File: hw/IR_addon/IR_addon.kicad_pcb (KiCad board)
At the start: 2 copper layers, 89.6 x 55 mm, 90 parts, among them J1 CONN_02X08, J10 CONN_01X01, J11 CONN_01X01, J12 CONN_01X01, J13 CONN_01X01, J14 CONN_01X01, J15 CONN_01X01, J16 CONN_01X01, J17 CONN_01X01, J18 CONN_01X01, J19 CONN_01X01, J2 CONN_02X08, J20 CONN_01X01, J21 CONN_01X01, J22 CONN_01X01, J23 CONN_01X01, J24 CONN_01X01, J25 CONN_01X01, J26 CONN_01X01, J27 CONN_01X01, J28 CONN_01X01, J29 CONN_01X01, J3 CONN_01X02, J30 CONN_01X01, J31 CONN_01X01, J32 CONN_01X01, J33 CONN_01X01, J34 CONN_01X01, J35 CONN_01X01, J36 CONN_01X01, J37 CONN_01X01, J38 CONN_01X01, J39 CONN_01X01, J40 CONN_01X01, J41 CONN_02X03, J42 CONN_01X15, J43 CONN_01X15, J44 USB_B_Mini, J9 CONN_01X01, SW1 SwitchPush, U1 ATmega328P-AU, U2 FT230XQ, Y1 16MHz

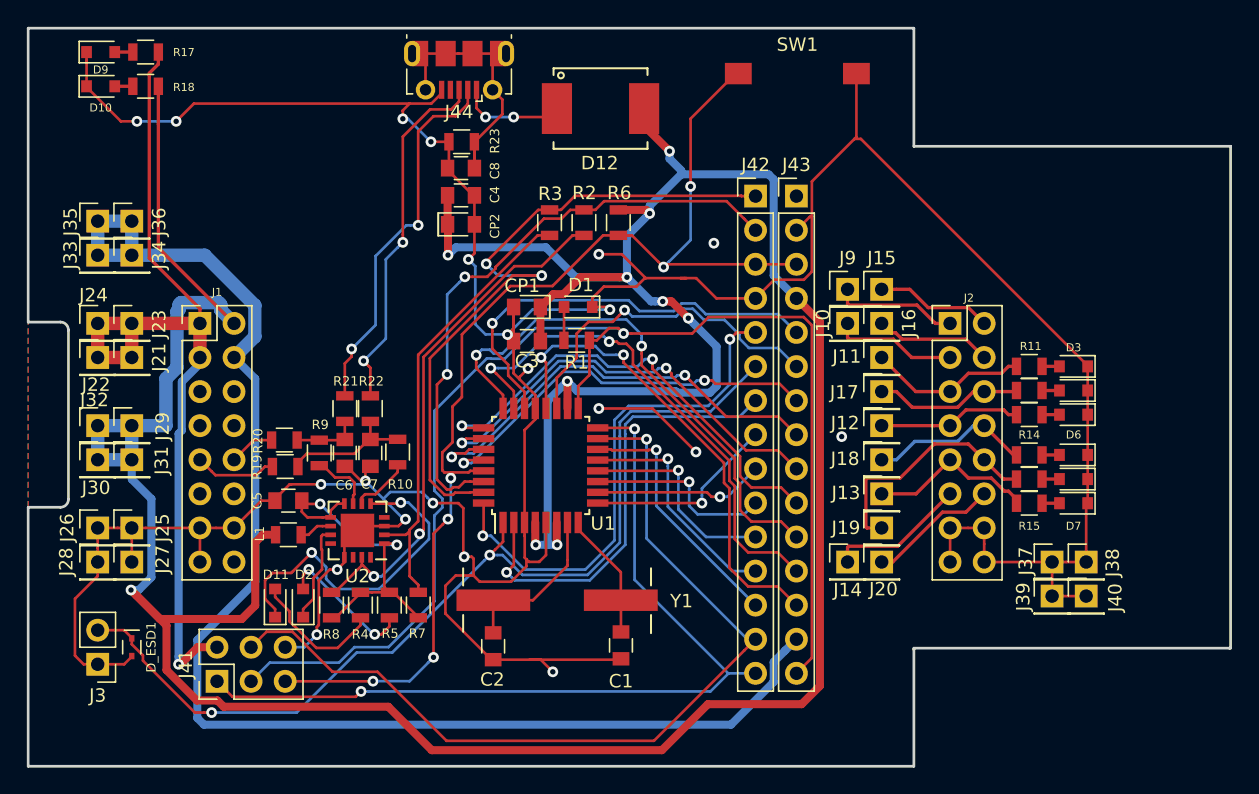
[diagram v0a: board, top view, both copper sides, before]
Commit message: Various fixes in schematics and PCB design
What has been done:

* Replace FT230XQ with FT232RQ
* Adapt schematics to new FTDI chip
* Rearrange texts on F.Mask layer
* Add smaller schottky diode next to usb
* Add load resistor for IR LED
* Move capacitors further from XTAL
* Rearrange overlapping texts on F.Silk layer

Doubts:

* Maybe we should remove uUSB from PCB, since all we are using
  are USB lines from MuxPi. As for now uUSB was never used.

Change-Id: Icd19173fda610c0574442d99b39109bb18bf1090
Signed-off-by: Katarzyna Gorska <k.gorska@samsung.com>
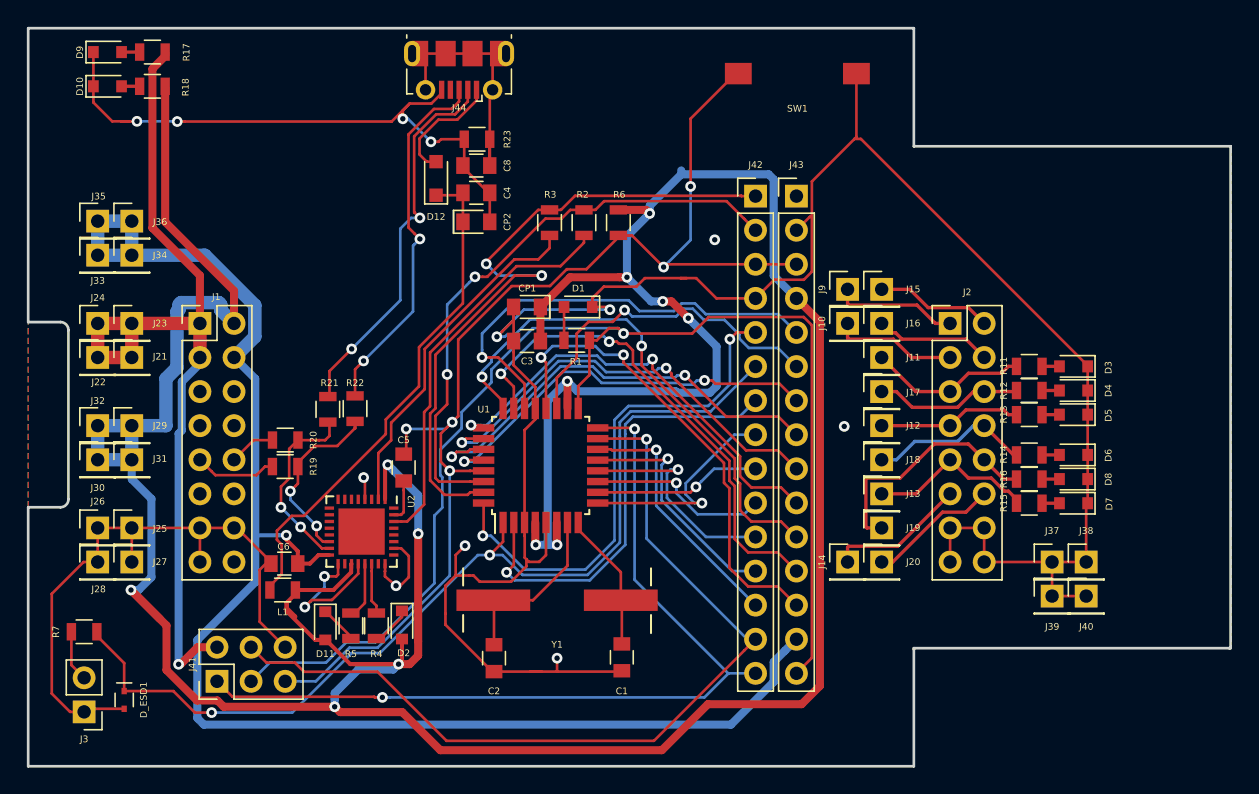
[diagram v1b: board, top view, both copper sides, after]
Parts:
- removed C7: 47pF/50V, Muxpi Addon:C_0805
- removed R10, R9: 27R, Muxpi Addon:R_0805
- removed R8: 10k, Muxpi Addon:R_0805
- C1, C2, C3, C4, C5, C8: footprint Muxpi Addon:C_0805 -> Muxpi_footprints:C_0805
- C6: value 47pF/50V -> 0.1uF; footprint Muxpi Addon:C_0805 -> Muxpi_footprints:C_0805
- CP1, CP2: footprint Muxpi Addon:C_T_0805 -> Muxpi_footprints:C_T_0805
- D1, D10, D11, D3, D4, D5, D6, D7, D8, D9: footprint Diodes_SMD:D_0805 -> Muxpi_footprints:D_0805
- D12: value MBRS410L -> BAT60B; footprint Muxpi Addon:403AC -> Muxpi_footprints:D_SOD-323_HandSoldering
- D2: value KPT-2012SGC -> KPT-2012EC; footprint Diodes_SMD:D_0805 -> Muxpi_footprints:D_0805
- D_ESD1: footprint Muxpi Addon:SOD-523 -> Muxpi_footprints:SOD-523
- J1, J2: footprint Pin_Headers:Pin_Header_Straight_2x08_Pitch2.54mm -> Muxpi_footprints:Pin_Header_Straight_2x08_Pitch2.54mm
- J10, J11, J12, J13, J14, J15, J16, J17, J18, J19, J20, J21, J22, J23, J24, J25, J26, J27, J28, J29, J30, J31, J32, J33, J34, J35, J36, J37, J38, J39, J40, J9: footprint Pin_Headers:Pin_Header_Straight_1x01_Pitch2.54mm -> Muxpi_footprints:Pin_Header_Straight_1x01_Pitch2.54mm
- J3: footprint Pin_Headers:Pin_Header_Straight_1x02_Pitch2.54mm -> Muxpi_footprints:Pin_Header_Straight_1x02_Pitch2.54mm
- J41: footprint Muxpi Addon:Pin_Header_Straight_2x03_Pitch2.54mm -> Muxpi_footprints:Pin_Header_Straight_2x03_Pitch2.54mm
- J42, J43: footprint Muxpi Addon:Pin_Header_Straight_1x15_Pitch2.54mm -> Muxpi_footprints:Pin_Header_Straight_1x15_Pitch2.54mm
- J44: footprint Muxpi Addon:USB_Micro-B_Molex-105017-0001 -> Muxpi_footprints:USB_Micro-B_Molex-105017-0001
- L1, R1, R19, R2, R20, R22, R23, R3, R6: footprint Muxpi Addon:R_0805 -> Muxpi_footprints:R_0805
- R11, R12, R13, R14, R15, R16, R17, R18: footprint Resistors_SMD:R_0805 -> Muxpi_footprints:R_0805
- R21: value 0 -> 330R; footprint Muxpi Addon:R_0805 -> Muxpi_footprints:R_0805
- R4, R5: value 560R -> 330R; footprint Muxpi Addon:R_0805 -> Muxpi_footprints:R_0805
- R7: value 10k -> R; footprint Muxpi Addon:R_0805 -> Muxpi_footprints:R_0805
- SW1: footprint Muxpi Addon:DTSM-3 -> Muxpi_footprints:DTSM-3
- U1: footprint Muxpi Addon:TQFP-32_7x7mm_Pitch0.8mm -> Muxpi_footprints:TQFP-32_7x7mm_Pitch0.8mm
- U2: value FT230XQ -> FT232RQ; footprint Muxpi Addon:QFN-16-1EP_4x4mm_Pitch0.65mm -> Muxpi_footprints:QFN-32-1EP_5x5mm_Pitch0.5mm
- Y1: footprint Muxpi Addon:HC49USM -> Muxpi_footprints:HC49USM
- moved R7 25.0 mm to (73.5, 179.6), turned to 180 degrees
- moved D12 13.3 mm to (99.7, 145.8), turned to 90 degrees
- moved C6 9.40 mm to (88.4, 174.5), turned to 180 degrees
- moved C5 8.94 mm to (97.3, 167.3), turned to 90 degrees
- moved D2 7.55 mm to (97.2, 179.1), turned to 270 degrees
- moved L1 4.14 mm to (88.3, 176.5)
- moved D11 4.10 mm to (91.4, 179.1), turned to 270 degrees
- moved D_ESD1 3.97 mm to (76.5, 184.7)
- moved J3 3.69 mm to (73.5, 185.5)
- moved R5 3.26 mm to (93.3, 179.1)
- moved R4 1.95 mm to (95.2, 179.1)
- moved R21 1.27 mm to (91.6, 163.0), turned to 90 degrees
- moved C4 1.16 mm to (102.7, 146.9)
- moved C8 1.16 mm to (102.7, 144.8)
- moved CP2 1.16 mm to (102.7, 149.0)
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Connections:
- C4 pad 1: VDD -> Net-(C4-Pad1)
- C5 pad 2: GND -> /RESET
- C6 pad 1: Net-(C6-Pad1) -> +3V3
- CP2 pad 1: VDD -> Net-(C4-Pad1)
- D11 pad 2: Net-(D11-Pad2) -> VDD
- D12 pad 1: Net-(D12-Pad1) -> Net-(C4-Pad1)
- D12 pad 2: VDD -> Net-(D12-Pad2)
- D2 pad 2: Net-(D2-Pad2) -> VDD
- J3 pad 2: /D3 -> Net-(J3-Pad2)
- J44 pad 1: Net-(D12-Pad1) -> Net-(D12-Pad2)
- L1 pad 1: Net-(L1-Pad1) -> VDD
- L1 pad 2: VDD -> Net-(C4-Pad1)
- R19 pad 1: Net-(C7-Pad1) -> Net-(R19-Pad1)
- R20 pad 1: Net-(C6-Pad1) -> /USB_B-
- R20 pad 2: /USB_B- -> Net-(R20-Pad2)
- R21 pad 1: /USB_C- -> Net-(R20-Pad2)
- R21 pad 2: Net-(C6-Pad1) -> /USB_C-
- R22 pad 2: Net-(C7-Pad1) -> Net-(R19-Pad1)
- R4 pad 1: Net-(C5-Pad1) -> Net-(R4-Pad1)
- R4 pad 2: Net-(D11-Pad2) -> Net-(D2-Pad1)
- R5 pad 1: Net-(C5-Pad1) -> Net-(R5-Pad1)
- R5 pad 2: Net-(D2-Pad2) -> Net-(D11-Pad1)
- R7 pad 1: /TX -> /D3
- R7 pad 2: Net-(C5-Pad1) -> Net-(J3-Pad2)
- U2 pad 1: Net-(C5-Pad1) -> VDD
- U2 pad 10: Net-(L1-Pad1) -> Net-(U2-Pad10)
- U2 pad 11: Net-(D2-Pad1) -> Net-(U2-Pad11)
- U2 pad 12: Net-(U2-Pad12) -> (no net)
- U2 pad 13: GND -> (no net)
- U2 pad 14: Net-(U2-Pad14) -> Net-(R19-Pad1)
- U2 pad 15: /RX -> Net-(R20-Pad2)
- U2 pad 16: Net-(U2-Pad16) -> +3V3
- U2 pad 3: GND -> Net-(U2-Pad3)
- U2 pad 4: Net-(U2-Pad4) -> GND
- U2 pad 5: Net-(D11-Pad1) -> (no net)
- U2 pad 8: Net-(C5-Pad1) -> Net-(U2-Pad8)
- U2 pad 9: Net-(C5-Pad1) -> Net-(U2-Pad9)
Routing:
- net Net-(C4-Pad1): track 0.00 -> 37.9 mm
- net GND: track 307.9 -> 276.4 mm, vias 21 -> 14
- net Net-(C5-Pad1): track 26.2 -> 3.15 mm, vias 2 -> 0
- net Net-(D11-Pad1): track 25.5 -> 2.82 mm, vias 2 -> 0
- net Net-(R19-Pad1): track 0.00 -> 14.0 mm, vias 0 -> 2
- net Net-(R20-Pad2): track 0.00 -> 13.6 mm, vias 0 -> 2
- net VDD: track 272.2 -> 283.4 mm, vias 10 -> 12
- net Net-(D2-Pad2): track 10.5 -> 0.00 mm, vias 2 -> 0
- net Net-(D11-Pad2): track 10.2 -> 0.00 mm
- net Net-(C7-Pad1): track 9.80 -> 0.00 mm
- net /RX: track 38.8 -> 29.7 mm, vias 2 -> 0
- net Net-(D12-Pad2): track 0.00 -> 8.86 mm
- net Net-(D12-Pad1): track 7.89 -> 0.00 mm, vias 2 -> 0
- net +3V3: track 103.1 -> 110.7 mm, vias 0 -> 1
- net /TX: track 34.0 -> 26.6 mm
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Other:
- board text removed: "SCL"
- board text removed: "SDA"
- board text removed: "UA+"
- board text removed: "UA-"
- board text removed: "UB+"
- board text removed: "UB-"
